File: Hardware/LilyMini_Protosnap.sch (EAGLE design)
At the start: 68 parts, among them Q1 ZXMP6A13F, U1 SAMD11D14A-M, U2 AP2112K-3.3V, U3 ALS-PT19, Y1 32.768kHz

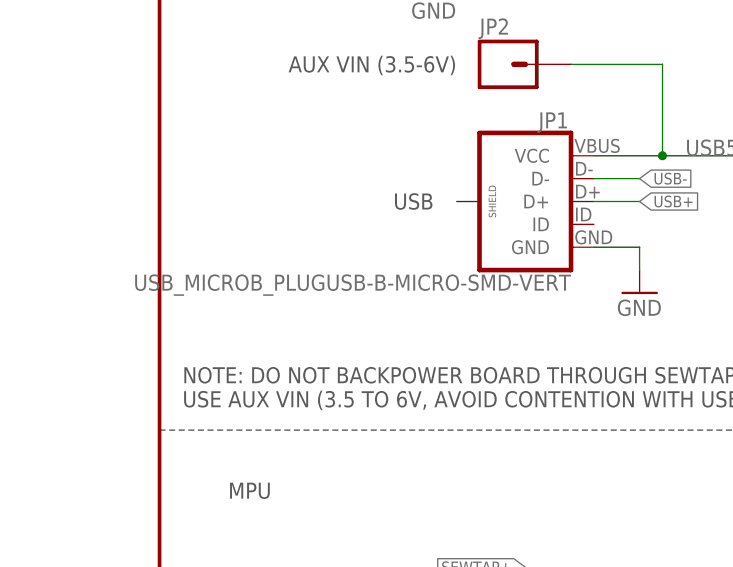
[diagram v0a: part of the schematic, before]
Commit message: Changed mouse bites from 0.02 to 0.015
Per Advanced Circuits, annular around original 0.02 drill hits would
reduce trace to hairline. Drills reduced to 0.015 to reduce this issue.
Smaller drills may make snapping harder, evaluate on proto.
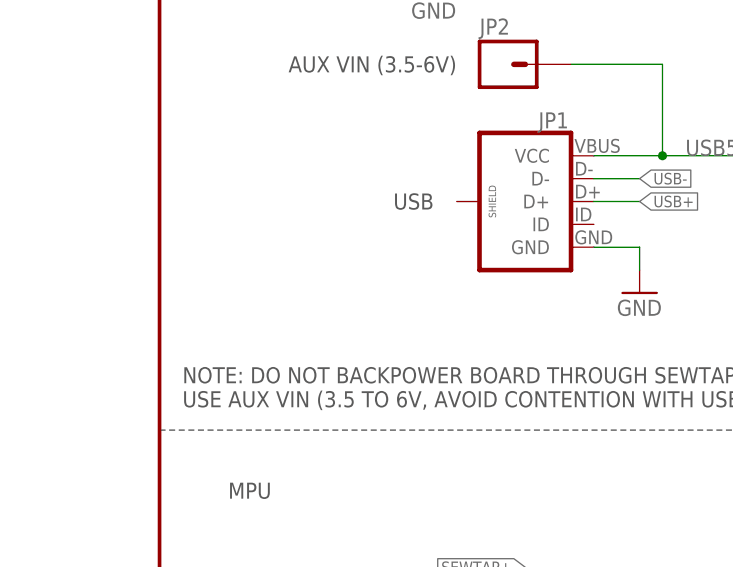
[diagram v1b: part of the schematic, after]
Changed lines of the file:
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@@
 <parts>
 <part name="FRAME1" library="SparkFun-Aesthetics" deviceset="FRAME-LETTER" device=""/>
-<part name="JP1" library="mike-temp" deviceset="USB_MICROB_PLUG" device="USB-B-MICRO-SMD-VERT" value="USB_MICROB_PLUGUSB-B-MICRO-SMD-VERT"/>
+<part name="JP1" library="mike-temp" deviceset="USB_MICROB_PLUG" device="USB-B-MICRO-SMD-VERT" value=""/>
 <part name="GND4" library="SparkFun-Aesthetics" deviceset="GND" device=""/>
 <part name="SUPPLY3" library="SparkFun-Aesthetics" deviceset="VDD" device=""/>

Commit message: Minor changes pre review
Enlarged copper on programming pins
Added VBATT3 test point
Added TDOCU text for test points
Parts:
- added JP10: (no value), mike-temp:M01_POGOPAD_20M_NS_1S_ROUND
- U3: device mike-temp:LIGHTSENSORALS -> SparkFun-Sensors:LIGHTSENSORALS
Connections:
- net BATT3V: now also JP10.1
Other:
- note added: "02"
- note removed: "01"
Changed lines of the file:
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@@
 <part name="SEWTAPLSOUT" library="LilyPad-Wearables" deviceset="SEWTAP" device="6" value="OUT"/>
 <part name="R6" library="SparkFun-Resistors" deviceset="10KOHM-1/10W-1%(0603)" device="0603" value="10K"/>
-<part name="U3" library="mike-temp" deviceset="LIGHTSENSOR" device="ALS" value="ALS-PT19"/>
+<part name="U3" library="SparkFun-Sensors" deviceset="LIGHTSENSOR" device="ALS" value="ALS-PT19"/>
 <part name="D3" library="SparkFun-LED" deviceset="LED-WHITE" device="1206"/>
 <part name="D4" library="SparkFun-LED" deviceset="LED-WHITE" device="1206"/>
@@
 <part name="FD4" library="SparkFun-Aesthetics" deviceset="FIDUCIAL" device="UFIDUCIAL"/>
 <part name="LOGO4" library="SparkFun-Aesthetics" deviceset="SFE_LOGO_NAME" device=".1_INCH"/>
+<part name="JP10" library="mike-temp" deviceset="M01" device="_POGOPAD_20M_NS_1S_ROUND"/>
 </parts>
 <sheets>
@@
 SEWTAPS</text>
 <text x="165.1" y="7.62" size="2.54" layer="94">Mike Grusin and Angela Sheehan</text>
-<text x="243.84" y="7.62" size="2.54" layer="94">01</text>
+<text x="243.84" y="7.62" size="2.54" layer="94">02</text>
 <text x="106.68" y="40.64" size="1.778" layer="97">LILYMINI SEWTAPS</text>
 <text x="58.42" y="91.44" size="1.778" layer="97">S01</text>
@@
 <instance part="FD4" gate="G$1" x="246.38" y="30.48"/>
 <instance part="LOGO4" gate="G$1" x="154.94" y="35.56"/>
+<instance part="JP10" gate="G$1" x="200.66" y="55.88" smashed="yes" rot="R180">
+<attribute name="VALUE" x="203.2" y="60.96" size="1.778" layer="96" rot="R180"/>
+<attribute name="NAME" x="195.58" y="56.642" size="1.778" layer="95" rot="MR0"/>
+</instance>
 </instances>
 <busses>
@@
 <wire x1="45.72" y1="167.64" x2="66.04" y2="167.64" width="0.1524" layer="91"/>
 </segment>
-</net>
+<segment>
+<pinref part="JP10" gate="G$1" pin="1"/>
+<wire x1="193.04" y1="55.88" x2="185.42" y2="55.88" width="0.1524" layer="91"/>
+<label x="185.42" y="55.88" size="1.27" layer="95" rot="R180" xref="yes"/>
+</segment>
+</net>

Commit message: Minor updates
Larger fiducials
Sep version numbers on snap (1), LilyMini (1), light (2 - layout and
part change from current)
Added perforations
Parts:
- FD1, FD2, FD3, FD4: value FIDUCIALUFIDUCIAL -> FIDUCIAL1X2; device SparkFun-Aesthetics:FIDUCIALUFIDUCIAL -> SparkFun-Aesthetics:FIDUCIAL1X2
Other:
- note added: "10"
- note removed: "02"
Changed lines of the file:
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@@
 <setting verticaltext="up"/>
 </settings>
-<grid distance="0.1" unitdist="inch" unit="inch" style="lines" multiple="1" display="no" altdistance="0.01" altunitdist="inch" altunit="inch"/>
+<grid distance="0.1" unitdist="inch" unit="inch" style="lines" multiple="1" display="no" altdistance="0.05" altunitdist="inch" altunit="inch"/>
 <layers>
 <layer number="1" name="Top" color="4" fill="1" visible="no" active="no"/>
@@
 <part name="JP26" library="LilyPad-Wearables" deviceset="SEWTAP" device="6" value=""/>
 <part name="GND11" library="SparkFun-Aesthetics" deviceset="GND" device=""/>
-<part name="FD2" library="SparkFun-Aesthetics" deviceset="FIDUCIAL" device="UFIDUCIAL"/>
-<part name="FD1" library="SparkFun-Aesthetics" deviceset="FIDUCIAL" device="UFIDUCIAL"/>
-<part name="FD3" library="SparkFun-Aesthetics" deviceset="FIDUCIAL" device="UFIDUCIAL"/>
-<part name="FD4" library="SparkFun-Aesthetics" deviceset="FIDUCIAL" device="UFIDUCIAL"/>
+<part name="FD2" library="SparkFun-Aesthetics" deviceset="FIDUCIAL" device="1X2" value="FIDUCIAL1X2"/>
+<part name="FD1" library="SparkFun-Aesthetics" deviceset="FIDUCIAL" device="1X2" value="FIDUCIAL1X2"/>
+<part name="FD3" library="SparkFun-Aesthetics" deviceset="FIDUCIAL" device="1X2" value="FIDUCIAL1X2"/>
+<part name="FD4" library="SparkFun-Aesthetics" deviceset="FIDUCIAL" device="1X2" value="FIDUCIAL1X2"/>
 <part name="LOGO4" library="SparkFun-Aesthetics" deviceset="SFE_LOGO_NAME" device=".1_INCH"/>
 <part name="JP10" library="mike-temp" deviceset="M01" device="_POGOPAD_20M_NS_1S_ROUND"/>
@@
 SEWTAPS</text>
 <text x="165.1" y="7.62" size="2.54" layer="94">Mike Grusin and Angela Sheehan</text>
-<text x="243.84" y="7.62" size="2.54" layer="94">02</text>
+<text x="242.57" y="6.35" size="2.54" layer="94">10</text>
 <text x="106.68" y="40.64" size="1.778" layer="97">LILYMINI SEWTAPS</text>
 <text x="58.42" y="91.44" size="1.778" layer="97">S01</text>

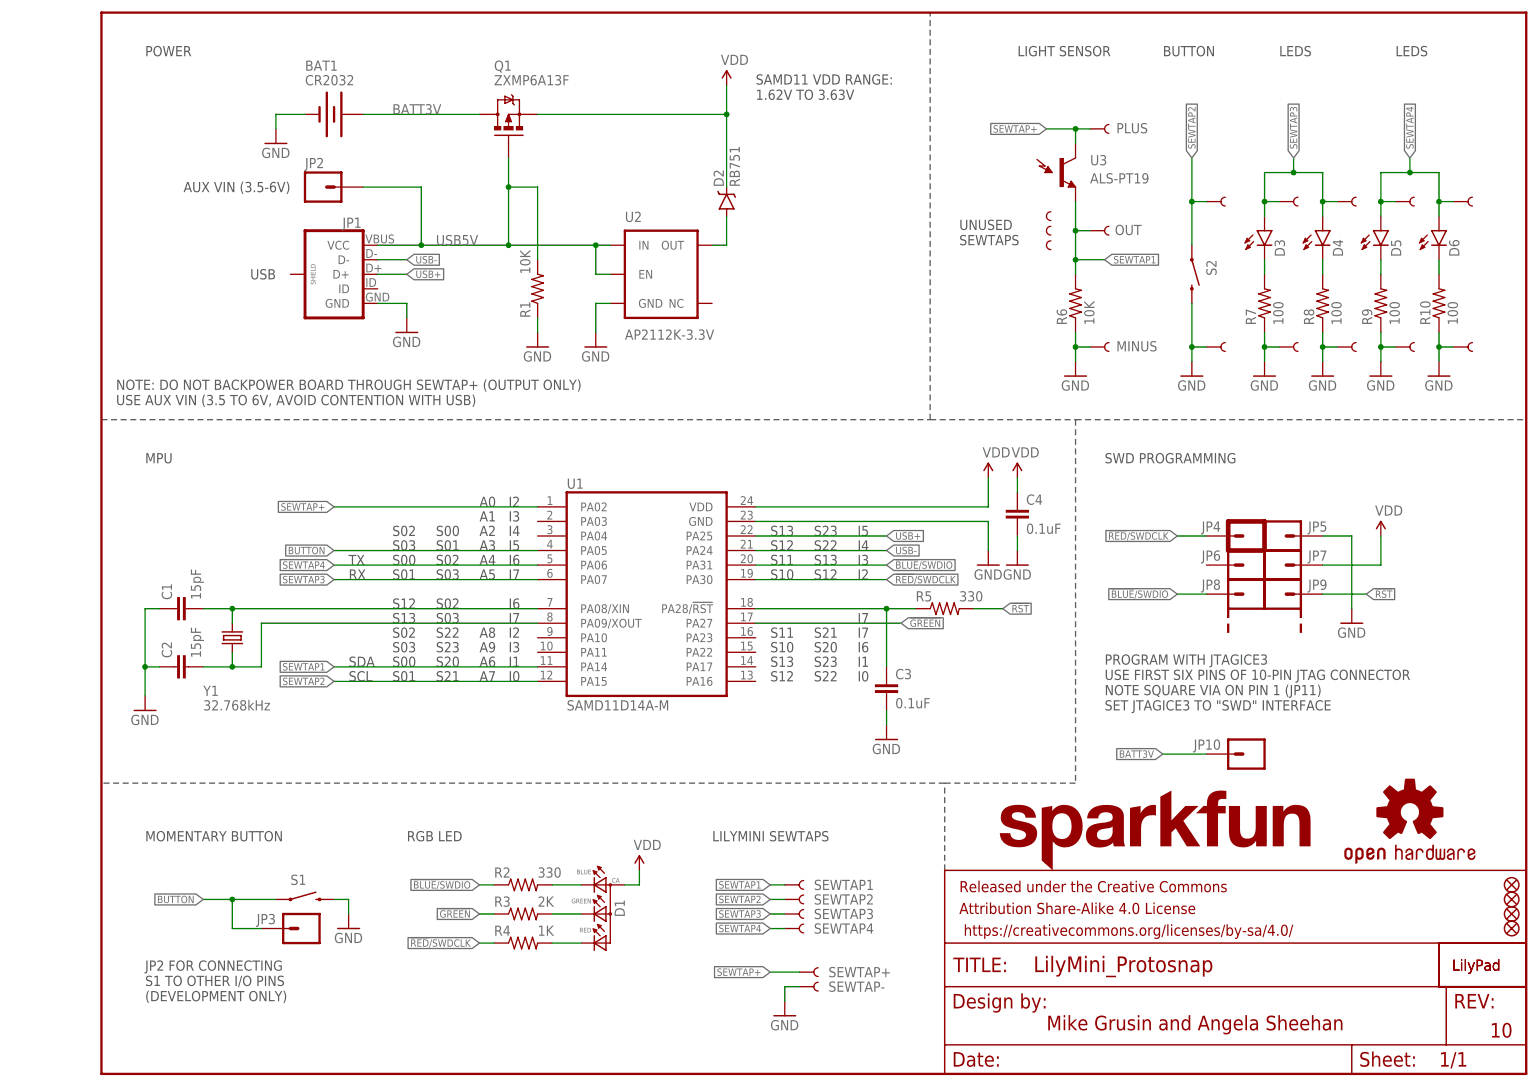
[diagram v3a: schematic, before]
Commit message: Changes per red review
LED resistors to 150 ohm
VBAT3V test point moved for selective solder
USB P/N lines moved to rear of board for clearance and impedance control
Perforations
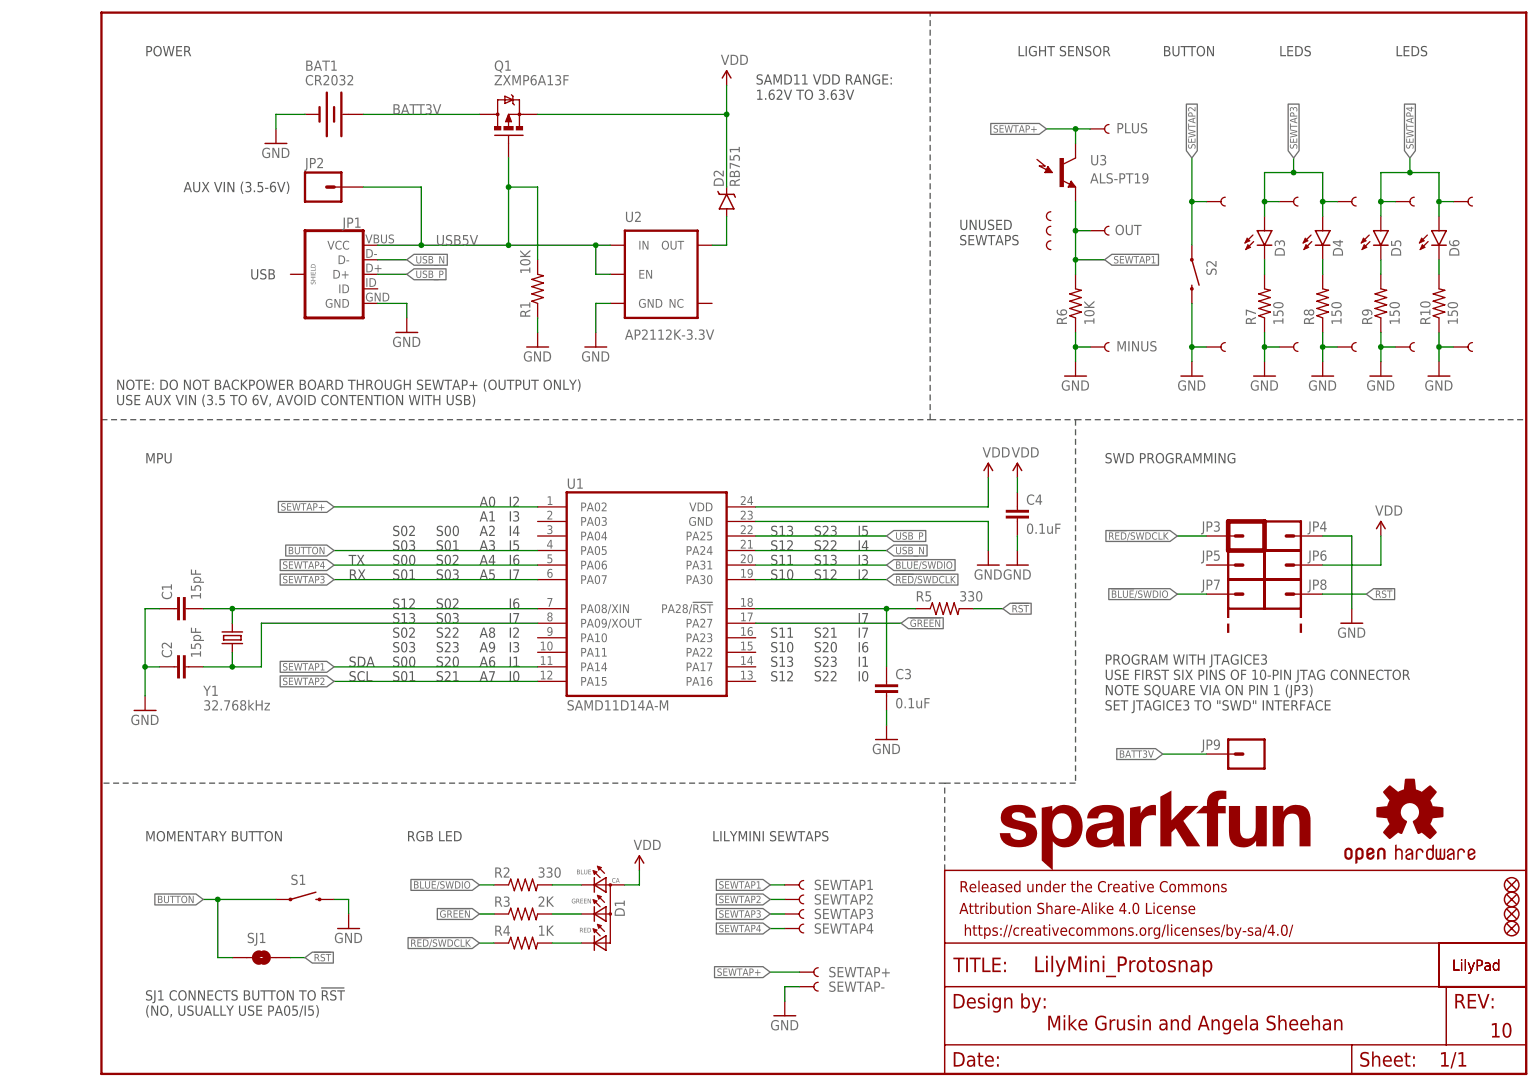
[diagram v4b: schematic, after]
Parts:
- removed JP10: (no value), mike-temp:M01_POGOPAD_20M_NS_1S_ROUND
- added SJ1: JUMPER-PAD-2-NO, SparkFun-Passives:JUMPER-PAD-2-NO
- JP3: device mike-temp:M01_POGOPAD_20M_NS_1S_ROUND -> mike-temp:M01_POGOPAD_20M_NS_1S_SQUARE
- JP4: device mike-temp:M01_POGOPAD_20M_NS_1S_SQUARE -> mike-temp:M01_POGOPAD_20M_NS_1S_ROUND
- R10, R7, R8, R9: value 100 -> 150; device SparkFun-Resistors:100OHM-1/10W-1%(0603) -> SparkFun-Resistors:RESISTOR0603
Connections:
- net USB+ renamed USB_P
- net USB- renamed USB_N
- net !BLUE!/SWDIO: now also JP7.1; no longer JP8.1
- net !RED!/SWDCLK: now also JP3.1; no longer JP4.1
- net !RST!: now also JP8.1, SJ1.2; no longer JP9.1
- net BATT3V: now also JP9.1; no longer JP10.1
- net BUTTON: now also SJ1.1; no longer JP3.1
- net GND: now also JP4.1; no longer JP5.1
- net VDD: now also JP6.1; no longer JP7.1
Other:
- note added: "PROGRAM WITH JTAGICE3 USE FIRST SIX PINS OF 10-PIN JTAG CONNECTOR NOTE SQUARE VIA ON PIN 1 (JP3) SET JTAGICE3 TO "SWD" INTERFACE"
- note added: "SJ1 CONNECTS BUTTON TO !RST! (NO, USUALLY USE PA05/I5)"
- note removed: "JP2 FOR CONNECTING S1 TO OTHER I/O PINS (DEVELOPMENT ONLY)"
- note removed: "PROGRAM WITH JTAGICE3 USE FIRST SIX PINS OF 10-PIN JTAG CONNECTOR NOTE SQUARE VIA ON PIN 1 (JP11) SET JTAGICE3 TO "SWD" INTERFACE"
- moved on the sheet: JP3, JP4, JP5, JP6, JP7, JP8, JP9
